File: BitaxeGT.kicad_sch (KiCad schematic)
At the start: 10 parts, among them J1 XT30

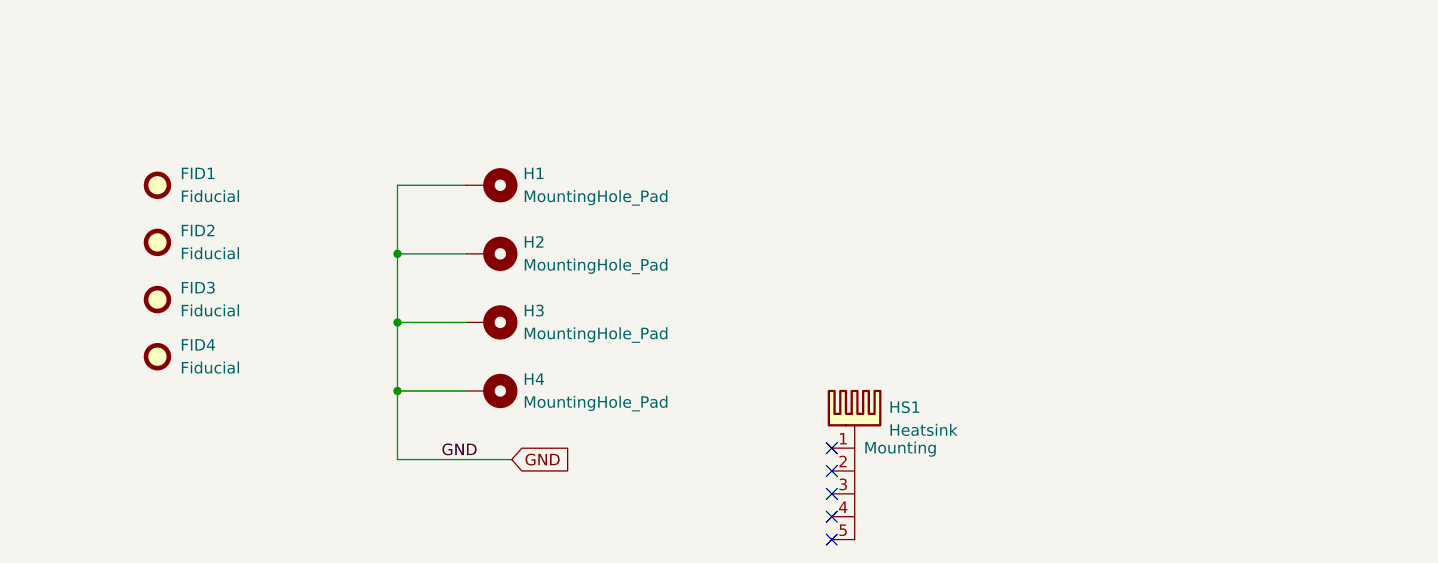
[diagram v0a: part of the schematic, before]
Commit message: Various changes in PCB
- Updated BM1370 footprint
- Added treaded spacers for heatsink
- Added component references on silkscreen
- Added PM logo
- Added BITAXE logo in solder mask expansion level
- Exported BOM and Gerber files
- Exported PCB 3D file
- Created production specs file
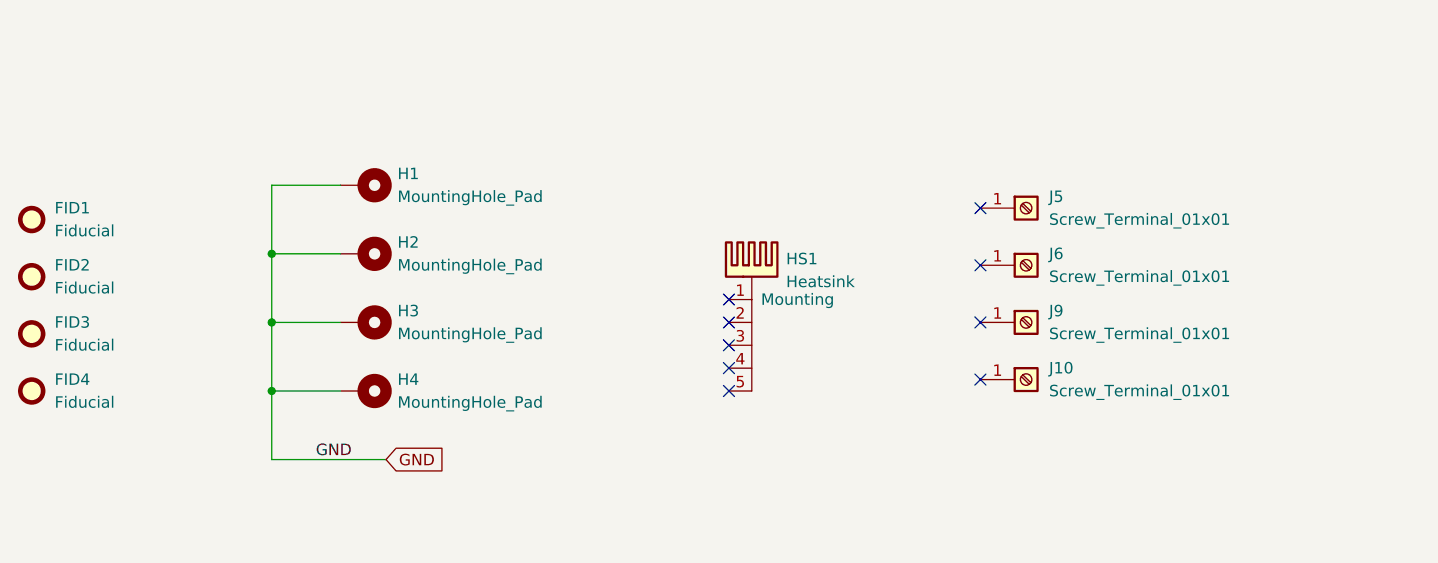
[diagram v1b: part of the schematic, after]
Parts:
- added J10, J5, J6, J9: Screw_Terminal_01x01, bitaxe:WA-SMSI_9774005360, symbol Connector:Screw_Terminal_01x01
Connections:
- no-connect marks 5 -> 9
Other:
- moved on the sheet: FID1, FID2, FID3, FID4, H1, H2, H3, H4, HS1
